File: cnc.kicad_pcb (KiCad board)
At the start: 2 copper layers, 25 parts, among them CON1 SD_Card, P1 USB_OTG, U1 pic32, U2 FOD817, U3 FOD817, U4 FOD817, U5 FOD817, U6 MCP2200, X1 CRYSTAL_SMD

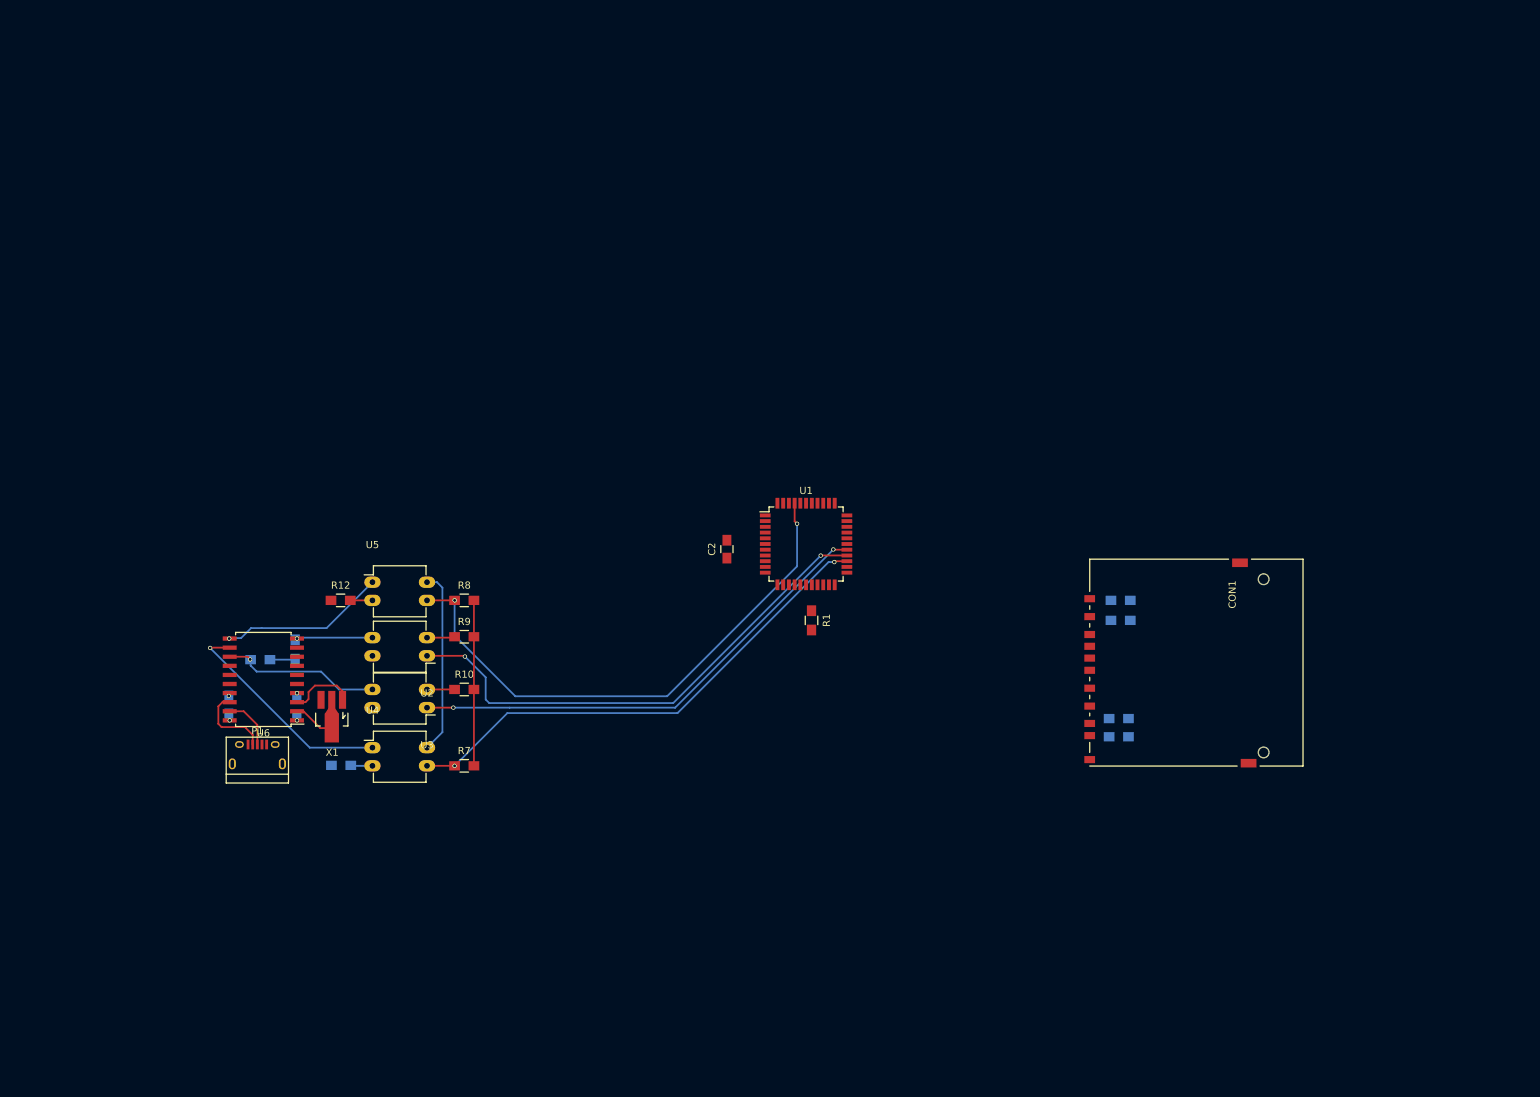
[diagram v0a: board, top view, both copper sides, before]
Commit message: added 3 more h-bridges, and routed a bit
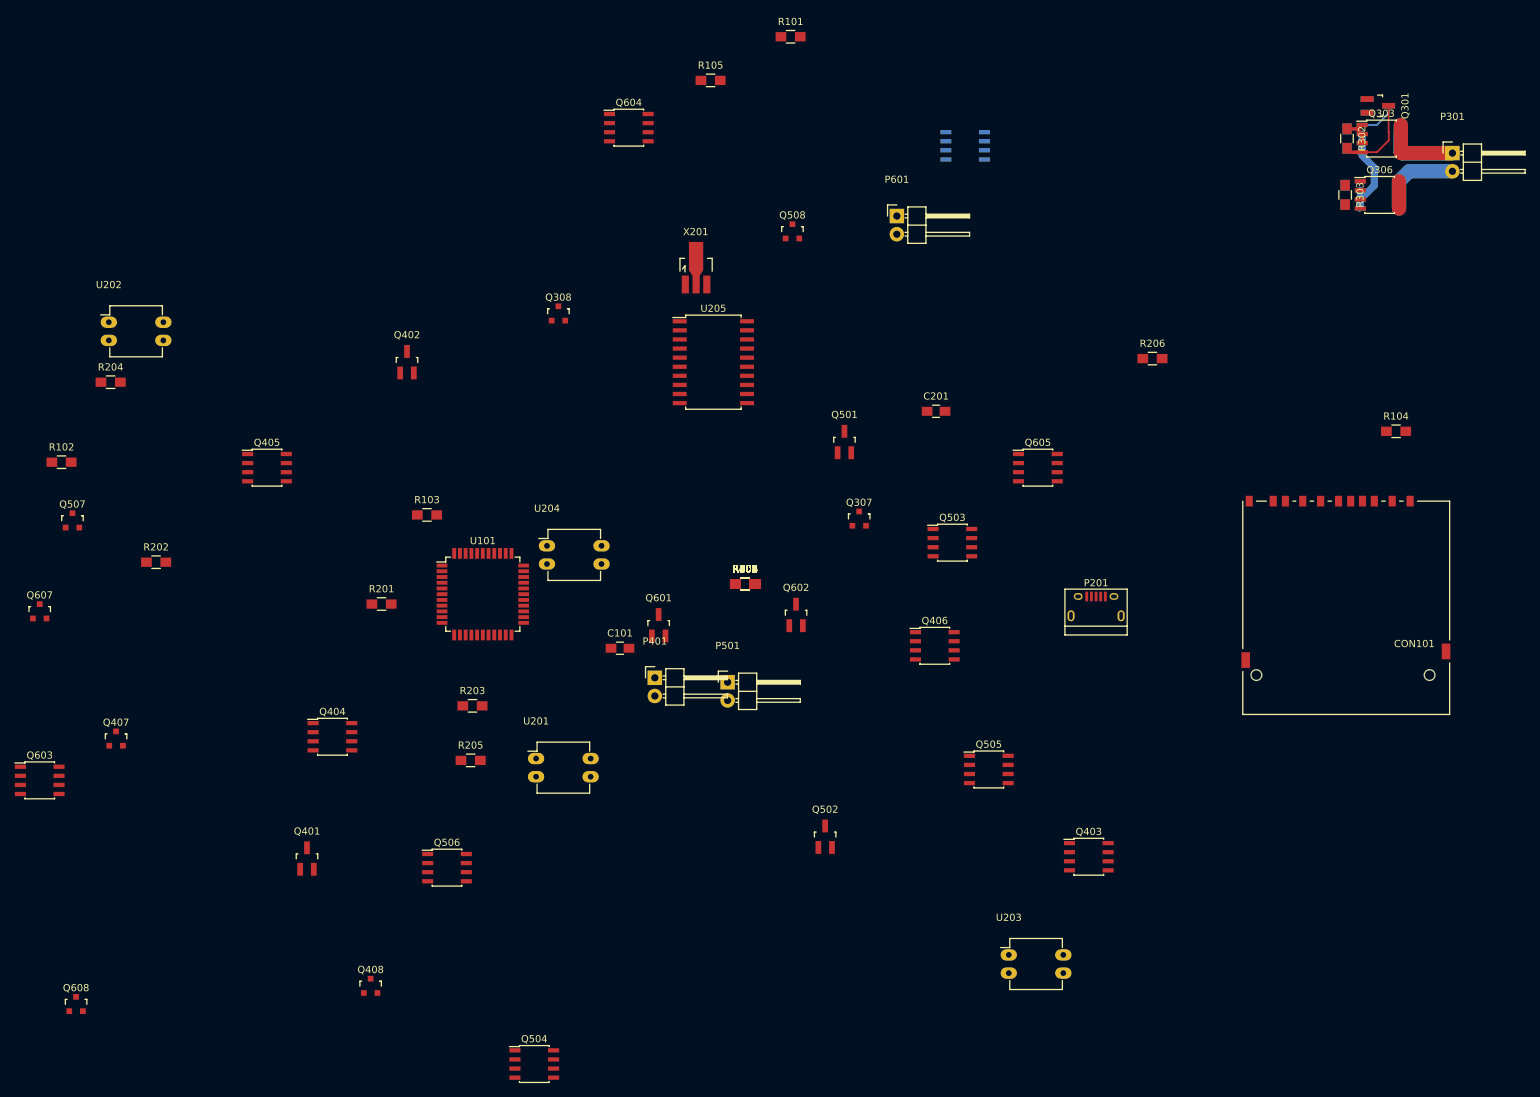
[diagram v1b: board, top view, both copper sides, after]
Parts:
- removed C1: C, Capacitors_SMD:C_0805_HandSoldering
- removed C2: 1uF, Capacitors_SMD:C_0805_HandSoldering
- removed CON1: SD_Card, Connect:SD_Card_Receptacle
- removed P1: USB_OTG, Connect:USB_Micro-B
- removed R1, R7, R8: 10k, Resistors_SMD:R_0805_HandSoldering
- removed R10, R11, R12, R13, R14, R15, R9: R, Resistors_SMD:R_0805_HandSoldering
- removed R3, R4, R5, R6: 50k, Resistors_SMD:R_0805_HandSoldering
- removed U1: pic32, Housings_QFP:TQFP-44_10x10mm_Pitch0.8mm
- removed U2, U3, U4, U5: FOD817, Housings_DIP:DIP-4_W7.62mm_LongPads
- removed U6: MCP2200, Housings_SOIC:SOIC-20_7.5x12.8mm_Pitch1.27mm
- removed X1: CRYSTAL_SMD, TO_SOT_Packages_SMD:SOT89-3_Housing_Handsoldering
- added C101: 1uF, Capacitors_SMD:C_0805_HandSoldering, F.Cu at (139.9, 106.5)
- added C201: C, Capacitors_SMD:C_0805_HandSoldering, F.Cu at (184.0, 73.4)
- added CON101: SD_Card, Connect:SD_Card_Receptacle, F.Cu at (240.9, 86.0)
- added P201: USB_OTG, Connect:USB_Micro-B, F.Cu at (206.4, 100.8)
- added P301: CONN_01X02, Pin_Headers:Pin_Header_Angled_1x02, F.Cu at (256.2, 37.3)
- added P401: CONN_01X02, Pin_Headers:Pin_Header_Angled_1x02, F.Cu at (144.7, 110.6)
- added P501: CONN_01X02, Pin_Headers:Pin_Header_Angled_1x02, F.Cu at (154.9, 111.3)
- added P601: CONN_01X02, Pin_Headers:Pin_Header_Angled_1x02, F.Cu at (178.5, 46.1)
- added Q301: Q_NMOS_GSD, TO_SOT_Packages_SMD:SOT-23_Handsoldering, F.Cu at (245.7, 30.7)
- added Q302: Q_NMOS_GSD, TO_SOT_Packages_SMD:SOT-23_Handsoldering, B.Cu at (245.7, 30.7)
- added Q303: IRF7606PBF, Housings_SOIC:SOIC-8_3.9x4.9mm_Pitch1.27mm, F.Cu at (246.3, 35.3)
- added Q304: IRF7607PBF, Housings_SOIC:SOIC-8_3.9x4.9mm_Pitch1.27mm, B.Cu at (246.3, 35.3)
- added Q305: IRF7607PBF, Housings_SOIC:SOIC-8_3.9x4.9mm_Pitch1.27mm, B.Cu at (246.0, 43.2)
- added Q306: IRF7606PBF, Housings_SOIC:SOIC-8_3.9x4.9mm_Pitch1.27mm, F.Cu at (246.0, 43.2)
- added Q307: Q_NMOS_GSD, TO_SOT_Packages_SMD:SOT-23, F.Cu at (173.3, 88.4)
- added Q308: Q_NMOS_GSD, TO_SOT_Packages_SMD:SOT-23, F.Cu at (131.3, 59.7)
- added Q401: Q_NMOS_GSD, TO_SOT_Packages_SMD:SOT-23_Handsoldering, F.Cu at (96.1, 135.9)
- added Q402: Q_NMOS_GSD, TO_SOT_Packages_SMD:SOT-23_Handsoldering, F.Cu at (110.1, 66.5)
- added Q403: IRF7606PBF, Housings_SOIC:SOIC-8_3.9x4.9mm_Pitch1.27mm, F.Cu at (205.4, 135.6)
- added Q404: IRF7607PBF, Housings_SOIC:SOIC-8_3.9x4.9mm_Pitch1.27mm, F.Cu at (99.7, 118.9)
- added Q405: IRF7607PBF, Housings_SOIC:SOIC-8_3.9x4.9mm_Pitch1.27mm, F.Cu at (90.6, 81.3)
- added Q406: IRF7606PBF, Housings_SOIC:SOIC-8_3.9x4.9mm_Pitch1.27mm, F.Cu at (183.8, 106.2)
- added Q407: Q_NMOS_GSD, TO_SOT_Packages_SMD:SOT-23, F.Cu at (69.5, 119.1)
- added Q408: Q_NMOS_GSD, TO_SOT_Packages_SMD:SOT-23, F.Cu at (105.0, 153.7)
- added Q501: Q_NMOS_GSD, TO_SOT_Packages_SMD:SOT-23_Handsoldering, F.Cu at (171.2, 77.7)
- added Q502: Q_NMOS_GSD, TO_SOT_Packages_SMD:SOT-23_Handsoldering, F.Cu at (168.5, 132.8)
- added Q503: IRF7606PBF, Housings_SOIC:SOIC-8_3.9x4.9mm_Pitch1.27mm, F.Cu at (186.3, 91.8)
- added Q504: IRF7607PBF, Housings_SOIC:SOIC-8_3.9x4.9mm_Pitch1.27mm, F.Cu at (127.9, 164.6)
- added Q505: IRF7607PBF, Housings_SOIC:SOIC-8_3.9x4.9mm_Pitch1.27mm, F.Cu at (191.4, 123.4)
- added Q506: IRF7606PBF, Housings_SOIC:SOIC-8_3.9x4.9mm_Pitch1.27mm, F.Cu at (115.7, 137.2)
- added Q507: Q_NMOS_GSD, TO_SOT_Packages_SMD:SOT-23, F.Cu at (63.4, 88.6)
- added Q508: Q_NMOS_GSD, TO_SOT_Packages_SMD:SOT-23, F.Cu at (164.0, 48.3)
- added Q601: Q_NMOS_GSD, TO_SOT_Packages_SMD:SOT-23_Handsoldering, F.Cu at (145.3, 103.3)
- added Q602: Q_NMOS_GSD, TO_SOT_Packages_SMD:SOT-23_Handsoldering, F.Cu at (164.5, 101.9)
- added Q603: IRF7606PBF, Housings_SOIC:SOIC-8_3.9x4.9mm_Pitch1.27mm, F.Cu at (58.8, 125.0)
- added Q604: IRF7607PBF, Housings_SOIC:SOIC-8_3.9x4.9mm_Pitch1.27mm, F.Cu at (141.1, 33.8)
- added Q605: IRF7607PBF, Housings_SOIC:SOIC-8_3.9x4.9mm_Pitch1.27mm, F.Cu at (198.2, 81.3)
- added Q606: IRF7606PBF, Housings_SOIC:SOIC-8_3.9x4.9mm_Pitch1.27mm, B.Cu at (188.1, 36.3)
- added Q607: Q_NMOS_GSD, TO_SOT_Packages_SMD:SOT-23, F.Cu at (58.8, 101.3)
- added Q608: Q_NMOS_GSD, TO_SOT_Packages_SMD:SOT-23, F.Cu at (63.9, 156.2)
- added R101: 10k, Resistors_SMD:R_0805_HandSoldering, F.Cu at (163.7, 21.1)
- added R102: 50k, Resistors_SMD:R_0805_HandSoldering, F.Cu at (61.8, 80.5)
- added R103: 50k, Resistors_SMD:R_0805_HandSoldering, F.Cu at (112.9, 87.9)
- added R104: 50k, Resistors_SMD:R_0805_HandSoldering, F.Cu at (248.3, 76.2)
- added R105: 50k, Resistors_SMD:R_0805_HandSoldering, F.Cu at (152.5, 27.2)
- added R201: 10k, Resistors_SMD:R_0805_HandSoldering, F.Cu at (106.6, 100.3)
- added R202: 10k, Resistors_SMD:R_0805_HandSoldering, F.Cu at (75.1, 94.5)
- added R203: R, Resistors_SMD:R_0805_HandSoldering, F.Cu at (119.3, 114.6)
- added R204: R, Resistors_SMD:R_0805_HandSoldering, F.Cu at (68.7, 69.3)
- added R205: R, Resistors_SMD:R_0805_HandSoldering, F.Cu at (119.0, 122.2)
- added R206: R, Resistors_SMD:R_0805_HandSoldering, F.Cu at (214.2, 66.0)
- added R207, R208, R209, R401, R402, R403, R404, R501, R502, R503, R504, R601, R602, R603, R604: R, Resistors_SMD:R_0805_HandSoldering, F.Cu at (157.3, 97.5)
- added R301: R, Resistors_SMD:R_0805_HandSoldering, B.Cu at (241.4, 35.3)
- added R302: R, Resistors_SMD:R_0805_HandSoldering, F.Cu at (241.4, 35.3)
- added R303: R, Resistors_SMD:R_0805_HandSoldering, F.Cu at (241.2, 43.2)
- added R304: R, Resistors_SMD:R_0805_HandSoldering, B.Cu at (241.2, 43.2)
- added U101: pic32, Housings_QFP:TQFP-44_10x10mm_Pitch0.8mm, F.Cu at (120.7, 99.0)
- added U201: FOD817, Housings_DIP:DIP-4_W7.62mm_LongPads, F.Cu at (128.1, 121.9)
- added U202: FOD817, Housings_DIP:DIP-4_W7.62mm_LongPads, F.Cu at (68.5, 61.0)
- added U203: FOD817, Housings_DIP:DIP-4_W7.62mm_LongPads, F.Cu at (194.2, 149.4)
- added U204: FOD817, Housings_DIP:DIP-4_W7.62mm_LongPads, F.Cu at (129.7, 92.2)
- added U205: MCP2200, Housings_SOIC:SOIC-20_7.5x12.8mm_Pitch1.27mm, F.Cu at (152.9, 66.5)
- added X201: CRYSTAL_SMD, TO_SOT_Packages_SMD:SOT89-3_Housing_Handsoldering, F.Cu at (150.5, 53.3)
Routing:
- net /uart/RTS: track 76.9 -> 0.00 mm, vias 2 -> 0
- net /uart/TX: track 71.7 -> 0.00 mm, vias 2 -> 0
- net /uart/RX: track 70.5 -> 0.00 mm, vias 2 -> 0
- net /uart/CTS: track 67.8 -> 0.00 mm, vias 2 -> 0
- net Net-(P301-Pad1): track 0.00 -> 33.2 mm
- net Net-(U4-Pad1): track 31.2 -> 0.00 mm, vias 1 -> 0
- net +3V3: track 25.7 -> 0.00 mm
- net Net-(U5-Pad1): track 23.3 -> 0.00 mm, vias 1 -> 0
- net GND: track 23.1 -> 0.00 mm
- net Net-(R13-Pad1): track 22.3 -> 0.00 mm, vias 1 -> 0
- net Net-(P301-Pad2): track 0.00 -> 18.2 mm
- net PWR_GND: track 0.00 -> 14.3 mm
- net Net-(Q301-Pad3): track 0.00 -> 11.6 mm
- net Net-(R14-Pad1): track 11.2 -> 0.00 mm, vias 1 -> 0
- net Net-(P1-Pad2): track 11.1 -> 0.00 mm
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
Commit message: Routed a h-bridge. Damn that's a lot of work.
also assigned a lot of components.
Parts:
- removed Q307, Q308, Q407, Q408, Q507, Q508, Q607, Q608: Q_NMOS_GSD, TO_SOT_Packages_SMD:SOT-23
- removed U201, U202, U203, U204: FOD817, Housings_DIP:DIP-4_W7.62mm_LongPads
- added C301: 15nF, lib:R_0402_handsoldering, F.Cu at (257.3, 30.5)
- added C302: 15nF, lib:R_0402_handsoldering, F.Cu at (258.1, 31.8)
- added C303: 15nF, lib:R_0402_handsoldering, B.Cu at (259.0, 20.3)
- added C304: 15nF, lib:R_0402_handsoldering, B.Cu at (256.9, 19.1)
- added C401: 15nF, lib:R_0402_handsoldering, F.Cu at (255.2, 51.2)
- added C402: 15nF, lib:R_0402_handsoldering, F.Cu at (256.9, 50.3)
- added C403: 15nF, lib:R_0402_handsoldering, B.Cu at (259.6, 43.6)
- added C404: 15nF, lib:R_0402_handsoldering, F.Cu at (257.8, 43.0)
- added C501, C502, C503, C504, C601, C602, C603, C604: 15nF, lib:R_0402_handsoldering, F.Cu at (211.3, 58.7)
- added C701: 100nF, lib:R_0402_handsoldering, F.Cu at (89.6, 114.3)
- added C702: 10uF, lib:R_0402_handsoldering, F.Cu at (211.3, 58.7)
- added C703: 10nF, lib:R_0402_handsoldering, B.Cu at (75.6, 116.3)
- added C704: 120uF, Capacitors_ThroughHole:C_Radial_D5_L11_P2.5, F.Cu at (68.7, 109.0)
- added D301: D, Diodes_SMD:SOD-323, F.Cu at (257.6, 33.6)
- added D302: D, Diodes_SMD:SOD-323, B.Cu at (257.3, 28.0)
- added D303: D, Diodes_SMD:SOD-323, B.Cu at (257.4, 22.7)
- added D304: D, Diodes_SMD:SOD-323, B.Cu at (255.4, 21.0)
- added D401: D, Diodes_SMD:SOD-323, B.Cu at (258.2, 54.5)
- added D402: D, Diodes_SMD:SOD-323, F.Cu at (258.0, 54.2)
- added D403: D, Diodes_SMD:SOD-323, F.Cu at (257.3, 45.5)
- added D404: D, Diodes_SMD:SOD-323, B.Cu at (256.7, 44.3)
- added D501: D, Diodes_SMD:SOD-323, F.Cu at (210.1, 61.0)
- added D502: D, Diodes_SMD:SOD-323, F.Cu at (210.7, 59.9)
- added D503: D, Diodes_SMD:SOD-323, F.Cu at (210.2, 60.1)
- added D504: D, Diodes_SMD:SOD-323, F.Cu at (210.6, 57.0)
- added D601: D, Diodes_SMD:SOD-323, F.Cu at (211.3, 58.7)
- added D602: D, Diodes_SMD:SOD-323, F.Cu at (210.0, 60.5)
- added D603: D, Diodes_SMD:SOD-323, F.Cu at (210.1, 56.7)
- added D604: D, Diodes_SMD:SOD-323, F.Cu at (207.9, 58.5)
- added D701: D_Schottky, Diodes_SMD:DO-214AB_Handsoldering, B.Cu at (75.1, 112.0)
- added L701: 15uH, lib:VLS6045EX_6x6, F.Cu at (75.2, 110.5)
- added P101: icsp, Pin_Headers:Pin_Header_Straight_1x05, F.Cu at (105.8, 87.6)
- added R1: 10k, lib:R_0402_handsoldering, F.Cu at (254.9, 30.4)
- added R2: 10k, lib:R_0402_handsoldering, F.Cu at (130.1, 97.0)
- added R3: 10k, lib:R_0402_handsoldering, F.Cu at (272.3, 95.8)
- added R305: 1k, lib:R_0402_handsoldering, F.Cu at (257.3, 28.3)
- added R306, R506, R507, R511, R606, R607, R611: 10k, lib:R_0402_handsoldering, F.Cu at (211.3, 58.7)
- added R307: 10k, lib:R_0402_handsoldering, F.Cu at (254.8, 18.7)
- added R308: 1k, lib:R_0402_handsoldering, F.Cu at (257.9, 22.7)
- added R309: 1k, lib:R_0402_handsoldering, B.Cu at (256.9, 21.0)
- added R310: 30R, lib:R_0402_handsoldering, B.Cu at (256.0, 24.1)
- added R311: 10k, lib:R_0402_handsoldering, B.Cu at (258.1, 24.5)
- added R4: 10k, lib:R_0402_handsoldering, F.Cu at (92.7, 41.9)
- added R405: 1k, lib:R_0402_handsoldering, B.Cu at (257.3, 52.8)
- added R406: 10k, lib:R_0402_handsoldering, B.Cu at (251.7, 38.2)
- added R407: 10k, lib:R_0402_handsoldering, F.Cu at (259.1, 38.9)
- added R408: 1k, lib:R_0402_handsoldering, F.Cu at (257.7, 44.3)
- added R409: 1k, lib:R_0402_handsoldering, F.Cu at (256.3, 43.7)
- added R410: 30R, lib:R_0402_handsoldering, B.Cu at (256.1, 47.1)
- added R411: 10k, lib:R_0402_handsoldering, B.Cu at (258.0, 47.2)
- added R505, R508, R509, R605, R608, R609: 1k, lib:R_0402_handsoldering, F.Cu at (211.3, 58.7)
- added R510, R610: 30R, lib:R_0402_handsoldering, F.Cu at (211.3, 58.7)
- added R701: 500k, lib:R_0402_handsoldering, B.Cu at (80.1, 119.6)
- added U1: ACPL-227, SMD_Packages:SOIC-8-N, F.Cu at (66.4, 54.4)
- added U2: ACPL-227, SMD_Packages:SOIC-8-N, F.Cu at (66.2, 60.7)
- added U701: LD1117S33TR, TO_SOT_Packages_SMD:SOT-223, F.Cu at (88.3, 109.0)
- added U702: LM22676, Housings_SOIC:SOIC-8-1EP_3.9x4.9mm_Pitch1.27mm, F.Cu at (75.6, 118.4)
- C201, P201, X201: moved to B.Cu
- P301, P401: footprint Pin_Headers:Pin_Header_Angled_1x02 -> Pin_Headers:Pin_Header_Straight_1x02; moved to B.Cu
- P501, P601: footprint Pin_Headers:Pin_Header_Angled_1x02 -> Pin_Headers:Pin_Header_Straight_1x02
- Q301: value Q_NMOS_GSD -> NTJD5121N; footprint TO_SOT_Packages_SMD:SOT-23_Handsoldering -> lib:SOT-363; moved to B.Cu
- Q302: value Q_NMOS_GSD -> IRF4905PbF; footprint TO_SOT_Packages_SMD:SOT-23_Handsoldering -> Power_Integrations:TO-220; moved to F.Cu
- Q303, Q403, Q503, Q603: value IRF7606PBF -> FQP85N06; footprint Housings_SOIC:SOIC-8_3.9x4.9mm_Pitch1.27mm -> Power_Integrations:TO-220
- Q304: value IRF7607PBF -> IRF4905PbF; footprint Housings_SOIC:SOIC-8_3.9x4.9mm_Pitch1.27mm -> Power_Integrations:TO-220; moved to F.Cu
- Q305: value IRF7607PBF -> FQP85N06; footprint Housings_SOIC:SOIC-8_3.9x4.9mm_Pitch1.27mm -> Power_Integrations:TO-220; moved to F.Cu
- Q306, Q406, Q506, Q606: value IRF7606PBF -> NTJD5121N; footprint Housings_SOIC:SOIC-8_3.9x4.9mm_Pitch1.27mm -> lib:SOT-363
- Q401, Q501, Q601: value Q_NMOS_GSD -> NTJD5121N; footprint TO_SOT_Packages_SMD:SOT-23_Handsoldering -> lib:SOT-363
- Q402, Q502, Q602: value Q_NMOS_GSD -> IRF4905PbF; footprint TO_SOT_Packages_SMD:SOT-23_Handsoldering -> Power_Integrations:TO-220
- Q404, Q504, Q604: value IRF7607PBF -> IRF4905PbF; footprint Housings_SOIC:SOIC-8_3.9x4.9mm_Pitch1.27mm -> Power_Integrations:TO-220
- Q405, Q505, Q605: value IRF7607PBF -> FQP85N06; footprint Housings_SOIC:SOIC-8_3.9x4.9mm_Pitch1.27mm -> Power_Integrations:TO-220
- R101, R102, R103, R104, R105, R201, R202, R203, R204: footprint Resistors_SMD:R_0805_HandSoldering -> lib:R_0402_handsoldering
- R205, R206, R207, R208, R209: footprint Resistors_SMD:R_0805_HandSoldering -> lib:R_0402_handsoldering; moved to B.Cu
- R301, R402, R501, R502, R601, R602: value R -> 10k; footprint Resistors_SMD:R_0805_HandSoldering -> lib:R_0402_handsoldering
- R302, R401: value R -> 10k; footprint Resistors_SMD:R_0805_HandSoldering -> lib:R_0402_handsoldering; moved to B.Cu
- R303, R503, R603: value R -> 30R; footprint Resistors_SMD:R_0805_HandSoldering -> lib:R_0402_handsoldering
- R304, R504, R604: value R -> 1k; footprint Resistors_SMD:R_0805_HandSoldering -> lib:R_0402_handsoldering
- R403: value R -> 30R; footprint Resistors_SMD:R_0805_HandSoldering -> lib:R_0402_handsoldering; moved to B.Cu
- R404: value R -> 1k; footprint Resistors_SMD:R_0805_HandSoldering -> lib:R_0402_handsoldering; moved to B.Cu
- moved Q603 206.5 mm to (264.3, 145.5)
- moved Q401 181.5 mm to (257.2, 52.1), turned to 180 degrees
- moved Q405 175.1 mm to (261.4, 42.8), turned to 270 degrees
- moved P201 170.6 mm to (43.5, 50.1), turned to 90 degrees
- moved Q404 170.3 mm to (252.1, 42.9), turned to 270 degrees
- moved R206 152.9 mm to (61.4, 60.2)
- moved Q604 148.7 mm to (265.6, 115.1)
- moved Q504 143.6 mm to (255.6, 99.0)
- moved Q402 142.5 mm to (252.1, 54.0), turned to 270 degrees
- moved P401 135.8 mm to (267.1, 51.8)
- moved C201 128.1 mm to (58.0, 50.0), turned to 270 degrees
- moved CON101 122.4 mm to (135.7, 148.6)
- moved Q506 116.1 mm to (220.9, 87.9)
- moved R209 114.1 mm to (53.0, 51.6), turned to 180 degrees
- moved R404 111.1 mm to (259.0, 52.7), turned to 270 degrees
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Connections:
- Q301 pad 1: /hbridge1/INA -> PWR_GND
- Q301 pad 2: PWR_GND -> Net-(C302-Pad1)
- Q302 pad 1: /hbridge1/INA -> Net-(Q301-Pad6)
- Q302 pad 2: PWR_GND -> Net-(P301-Pad1)
- Q302 pad 3: Net-(Q302-Pad3) -> Vpower
- Q303 pad 1: Vpower -> Net-(Q301-Pad3)
- Q303 pad 2: Vpower -> Net-(P301-Pad1)
- Q303 pad 3: Vpower -> PWR_GND
- Q304 pad 1: PWR_GND -> Net-(Q304-Pad1)
- Q304 pad 2: PWR_GND -> Net-(P301-Pad2)
- Q304 pad 3: PWR_GND -> Vpower
- Q305 pad 1: PWR_GND -> Net-(Q305-Pad1)
- Q305 pad 2: PWR_GND -> Net-(P301-Pad2)
- Q306 pad 1: Vpower -> PWR_GND
- Q306 pad 2: Vpower -> Net-(C303-Pad1)
- Q306 pad 3: Vpower -> Net-(Q305-Pad1)
- Q306 pad 4: Net-(Q306-Pad4) -> PWR_GND
- Q306 pad 5: Net-(P301-Pad2) -> Net-(C304-Pad1)
- Q306 pad 6: Net-(P301-Pad2) -> Net-(Q304-Pad1)
- Q401 pad 1: /hbridge2/INA -> PWR_GND
- Q401 pad 2: PWR_GND -> Net-(C402-Pad1)
- Q402 pad 1: /hbridge2/INA -> Net-(Q401-Pad6)
- Q402 pad 2: PWR_GND -> Net-(P401-Pad1)
- Q402 pad 3: Net-(Q402-Pad3) -> Vpower
- Q403 pad 1: Vpower -> Net-(Q401-Pad3)
- Q403 pad 2: Vpower -> Net-(P401-Pad1)
- Q403 pad 3: Vpower -> PWR_GND
- Q404 pad 1: PWR_GND -> Net-(Q404-Pad1)
- Q404 pad 2: PWR_GND -> Net-(P401-Pad2)
- Q404 pad 3: PWR_GND -> Vpower
- Q405 pad 1: PWR_GND -> Net-(Q405-Pad1)
- Q405 pad 2: PWR_GND -> Net-(P401-Pad2)
- Q406 pad 1: Vpower -> PWR_GND
- Q406 pad 2: Vpower -> Net-(C403-Pad1)
- Q406 pad 3: Vpower -> Net-(Q405-Pad1)
- Q406 pad 4: Net-(Q406-Pad4) -> PWR_GND
- Q406 pad 5: Net-(P401-Pad2) -> Net-(C404-Pad1)
- Q406 pad 6: Net-(P401-Pad2) -> Net-(Q404-Pad1)
- Q501 pad 1: /hbridge3/INA -> PWR_GND
- Q501 pad 2: PWR_GND -> Net-(C502-Pad1)
- Q502 pad 1: /hbridge3/INA -> Net-(Q501-Pad6)
- Q502 pad 2: PWR_GND -> Net-(P501-Pad1)
- Q502 pad 3: Net-(Q502-Pad3) -> Vpower
- Q503 pad 1: Vpower -> Net-(Q501-Pad3)
- Q503 pad 2: Vpower -> Net-(P501-Pad1)
- Q503 pad 3: Vpower -> PWR_GND
- Q504 pad 1: PWR_GND -> Net-(Q504-Pad1)
- Q504 pad 2: PWR_GND -> Net-(P501-Pad2)
- Q504 pad 3: PWR_GND -> Vpower
- Q505 pad 1: PWR_GND -> Net-(Q505-Pad1)
- Q505 pad 2: PWR_GND -> Net-(P501-Pad2)
- Q506 pad 1: Vpower -> PWR_GND
- Q506 pad 2: Vpower -> Net-(C503-Pad1)
- Q506 pad 3: Vpower -> Net-(Q505-Pad1)
- Q506 pad 4: Net-(Q506-Pad4) -> PWR_GND
- Q506 pad 5: Net-(P501-Pad2) -> Net-(C504-Pad1)
- Q506 pad 6: Net-(P501-Pad2) -> Net-(Q504-Pad1)
- Q601 pad 1: /hbridge4/INA -> PWR_GND
- Q601 pad 2: PWR_GND -> Net-(C602-Pad1)
- Q602 pad 1: /hbridge4/INA -> Net-(Q601-Pad6)
- Q602 pad 2: PWR_GND -> Net-(P601-Pad1)
- Q602 pad 3: Net-(Q602-Pad3) -> Vpower
- Q603 pad 1: Vpower -> Net-(Q601-Pad3)
- Q603 pad 2: Vpower -> Net-(P601-Pad1)
- Q603 pad 3: Vpower -> PWR_GND
- Q604 pad 1: PWR_GND -> Net-(Q604-Pad1)
- Q604 pad 2: PWR_GND -> Net-(P601-Pad2)
- Q604 pad 3: PWR_GND -> Vpower
- Q605 pad 1: PWR_GND -> Net-(Q605-Pad1)
- Q605 pad 2: PWR_GND -> Net-(P601-Pad2)
- Q606 pad 1: Vpower -> PWR_GND
- Q606 pad 2: Vpower -> Net-(C603-Pad1)
- Q606 pad 3: Vpower -> Net-(Q605-Pad1)
- Q606 pad 4: Net-(Q606-Pad4) -> PWR_GND
- Q606 pad 5: Net-(P601-Pad2) -> Net-(C604-Pad1)
- Q606 pad 6: Net-(P601-Pad2) -> Net-(Q604-Pad1)
- R301 pad 2: Net-(Q302-Pad3) -> Net-(Q301-Pad3)
- R302 pad 2: Net-(Q301-Pad3) -> Net-(Q301-Pad6)
- R303 pad 1: Vpower -> Net-(D301-Pad1)
- R303 pad 2: Net-(Q306-Pad4) -> /hbridge1/INA
- R304 pad 1: Vpower -> Net-(C302-Pad1)
- R304 pad 2: Net-(Q305-Pad4) -> Net-(D301-Pad1)
- R401 pad 2: Net-(Q402-Pad3) -> Net-(Q401-Pad3)
- R402 pad 2: Net-(Q401-Pad3) -> Net-(Q401-Pad6)
- R403 pad 1: Vpower -> Net-(D401-Pad1)
- R403 pad 2: Net-(Q406-Pad4) -> /hbridge2/INA
- R404 pad 1: Vpower -> Net-(C402-Pad1)
- R404 pad 2: Net-(Q405-Pad4) -> Net-(D401-Pad1)
- R501 pad 2: Net-(Q502-Pad3) -> Net-(Q501-Pad3)
- R502 pad 2: Net-(Q501-Pad3) -> Net-(Q501-Pad6)
- R503 pad 1: Vpower -> Net-(D501-Pad1)
- R503 pad 2: Net-(Q506-Pad4) -> /hbridge3/INA
- R504 pad 1: Vpower -> Net-(C502-Pad1)
- R504 pad 2: Net-(Q505-Pad4) -> Net-(D501-Pad1)
- R601 pad 2: Net-(Q602-Pad3) -> Net-(Q601-Pad3)
- R602 pad 2: Net-(Q601-Pad3) -> Net-(Q601-Pad6)
- R603 pad 1: Vpower -> Net-(D601-Pad1)
- R603 pad 2: Net-(Q606-Pad4) -> /hbridge4/INA
- R604 pad 1: Vpower -> Net-(C602-Pad1)
- R604 pad 2: Net-(Q605-Pad4) -> Net-(D601-Pad1)
- U101 pad 8: (no net) -> /pged
- U101 pad 9: (no net) -> /pgec
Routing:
- net PWR_GND: track 14.3 -> 99.6 mm, vias 0 -> 6
- net GND_USB: track 0.00 -> 67.6 mm, vias 0 -> 3
- net Vpower: track 4.70 -> 59.6 mm, vias 0 -> 1
- net Net-(P401-Pad2): track 0.00 -> 32.7 mm, vias 0 -> 1
- net /uart/V_USB: track 0.00 -> 32.0 mm, vias 0 -> 4
- net Net-(P401-Pad1): track 0.00 -> 30.8 mm
- net GND: track 0.00 -> 19.2 mm, vias 0 -> 1
- net +5V: track 0.00 -> 18.4 mm
- net Net-(P201-Pad3): track 0.00 -> 15.7 mm, vias 0 -> 1
- net Net-(R208-Pad1): track 0.00 -> 15.6 mm, vias 0 -> 2
- net Net-(P201-Pad2): track 0.00 -> 15.4 mm, vias 0 -> 1
- net Net-(Q401-Pad3): track 0.00 -> 13.4 mm
- net Net-(Q301-Pad6): track 0.00 -> 13.1 mm
- net Net-(C703-Pad1): track 0.00 -> 11.9 mm, vias 0 -> 3
- net Net-(P301-Pad2): track 18.2 -> 29.7 mm
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- added copper zone on B.Cu, net GND_USB
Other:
- board text added: "3"
- board text added: "4"
- board text added: "5"
- board text added: "6"
